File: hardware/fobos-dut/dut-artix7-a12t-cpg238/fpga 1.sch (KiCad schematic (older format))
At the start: 24 parts, among them U1 XC7A12T-CPG238, U9 IS25LP256D-JMLE

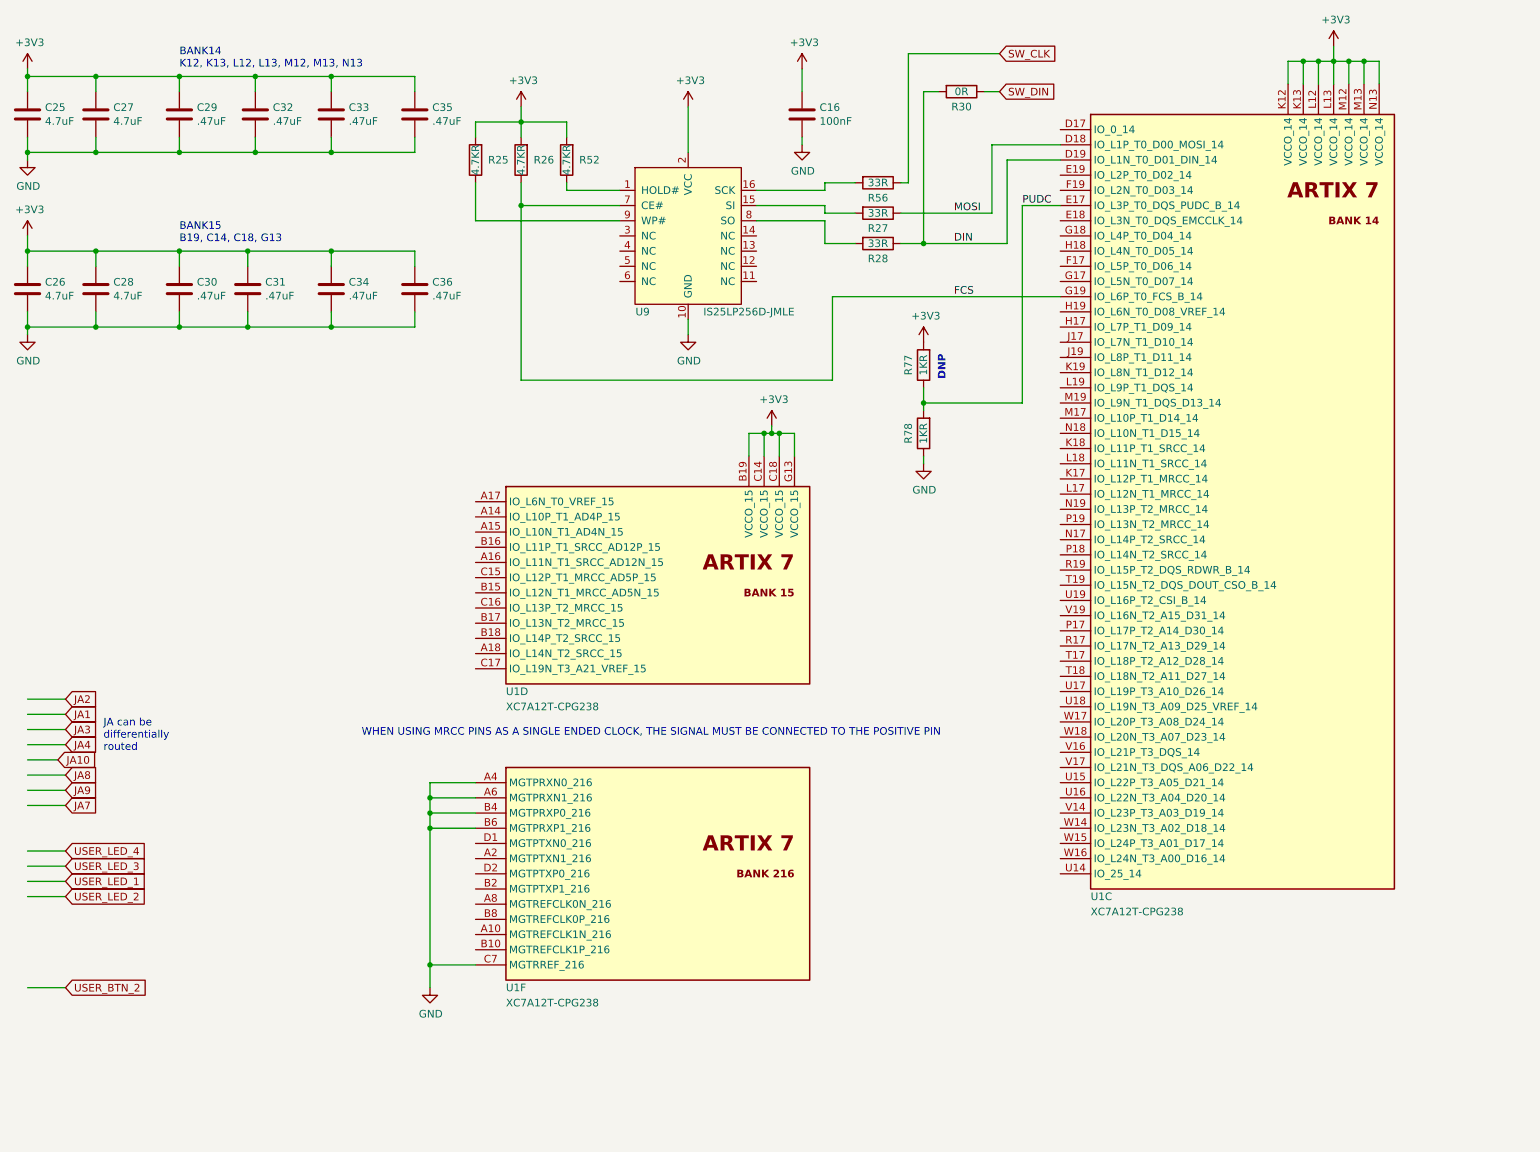
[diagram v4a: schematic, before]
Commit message: Updated escape routing of most pads to take advantage of "pad sacrifices"
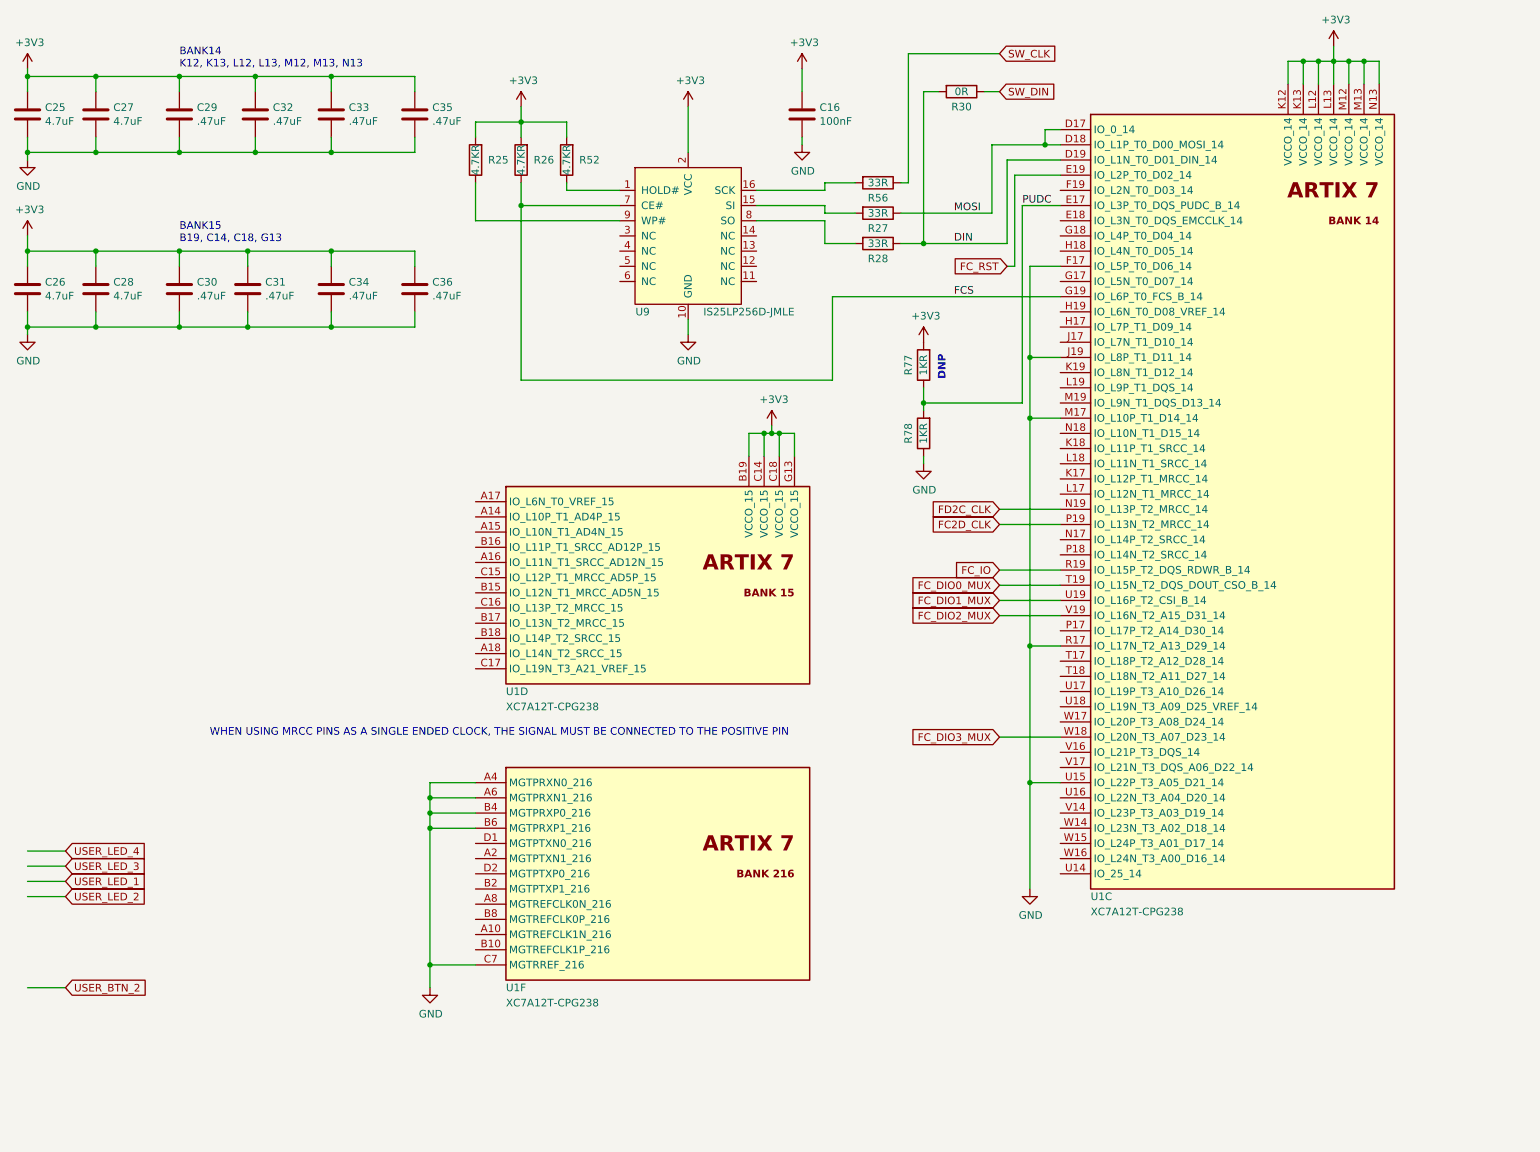
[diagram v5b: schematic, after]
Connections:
- net labels added: FC2D_CLK, FC_DIO0_MUX, FC_DIO1_MUX, FC_DIO2_MUX, FC_DIO3_MUX, FC_IO, FC_RST, FD2C_CLK
- net labels removed: JA1, JA10, JA2, JA3, JA4, JA7, JA8, JA9
- wire segments 142 -> 157
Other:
- note removed: "JA can be \ndifferentially\nrouted"
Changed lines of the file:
@@
 EndData
 $EndBitmap
-Text GLabel 900  5350 2    50   Input ~ 0
-JA1
-Text GLabel 900  5950 2    50   Input ~ 0
-JA7
-Text GLabel 900  5250 2    50   Input ~ 0
-JA2
-Text GLabel 900  5750 2    50   Input ~ 0
-JA8
-Text GLabel 900  5450 2    50   Input ~ 0
-JA3
-Text GLabel 900  5850 2    50   Input ~ 0
-JA9
-Text GLabel 900  5550 2    50   Input ~ 0
-JA4
-Wire Wire Line
-	900  5350 650  5350
-Wire Wire Line
-	650  5950 900  5950
-Wire Wire Line
-	650  5250 900  5250
-Wire Wire Line
-	900  5750 650  5750
-Wire Wire Line
-	900  5450 650  5450
-Wire Wire Line
-	900  5850 650  5850
-Wire Wire Line
-	900  5550 650  5550
-Text Notes 1150 5600 0    50   ~ 0
-JA can be \ndifferentially\nrouted
 $Comp
 L power:GND #PWR0124
@@
 Wire Wire Line
 	5750 1100 5750 1250
-Text GLabel 850  5650 2    50   Input ~ 0
-JA10
-Wire Wire Line
-	850  5650 650  5650
 Text GLabel 900  6250 2    50   Input ~ 0
 USER_LED_4
@@
 	7100 1700 7450 1700
 Wire Wire Line
-	7000 1600 7450 1600
+	7000 1600 7350 1600
 Text Notes 1650 2250 0    50   ~ 0
 BANK15\nB19, C14, C18, G13
@@
 Wire Wire Line
 	3300 7000 3300 7150
-Text Notes 2850 5500 0    50   ~ 0
+Text Notes 1850 5500 0    50   ~ 0
 WHEN USING MRCC PINS AS A SINGLE ENDED CLOCK, THE SIGNAL MUST BE CONNECTED TO THE POSITIVE PIN
 Text Label 6750 2050 0    50   ~ 0
@@
 Text Label 7200 2000 0    50   ~ 0
 PUDC
+Text GLabel 7050 4100 0    50   Input ~ 0
+FC2D_CLK
+Text GLabel 7050 4000 0    50   Input ~ 0
+FD2C_CLK
+Text GLabel 7100 2400 0    50   Input ~ 0
+FC_RST
+Wire Wire Line
+	7100 2400 7150 2400
+Wire Wire Line
+	7150 2400 7150 1800
+Wire Wire Line
+	7150 1800 7450 1800
+Text GLabel 7050 4400 0    50   Input ~ 0
+FC_IO
+Wire Wire Line
+	7050 4400 7450 4400
+Text GLabel 7050 4500 0    50   Input ~ 0
+FC_DIO0_MUX
+Wire Wire Line
+	7050 4500 7450 4500
+Wire Wire Line
+	7050 4000 7450 4000
+Wire Wire Line
+	7050 4100 7450 4100
+Text GLabel 7050 4600 0    50   Input ~ 0
+FC_DIO1_MUX
+Wire Wire Line
+	7450 4600 7050 4600
+Text GLabel 7050 4700 0    50   Input ~ 0
+FC_DIO2_MUX
+Wire Wire Line
+	7450 4700 7050 4700
+Text GLabel 7050 5500 0    50   Input ~ 0
+FC_DIO3_MUX
+Wire Wire Line
+	7450 5500 7050 5500
+$Comp
+L power:GND #PWR?
+U 1 1 61EE39A7
+P 7250 6500
+AR Path="/5F3A1954/61EE39A7" Ref="#PWR?"  Part="1"
+AR Path="/60D2F94F/61EE39A7" Ref="#PWR?"  Part="1"
+AR Path="/5F22D594/61EE39A7" Ref="#PWR0136"  Part="1"
+F 0 "#PWR0136" H 7250 6250 50  0001 C CNN
+F 1 "GND" H 7255 6327 50  0000 C CNN
+F 2 "" H 7250 6500 50  0001 C CNN
+F 3 "" H 7250 6500 50  0001 C CNN
+	1    7250 6500
+	1    0    0    -1
+$EndComp
+Wire Wire Line
+	7450 5800 7250 5800
+Wire Wire Line
+	7250 5800 7250 6500
+Wire Wire Line
+	7450 4900 7250 4900
+Wire Wire Line
+	7250 4900 7250 5800
+Connection ~ 7250 5800
+Wire Wire Line
+	7450 3400 7250 3400
+Wire Wire Line
+	7250 3400 7250 4900
+Connection ~ 7250 4900
+Wire Wire Line
+	7450 3000 7250 3000
+Wire Wire Line
+	7250 3000 7250 3400
+Connection ~ 7250 3400
+Wire Wire Line
+	7450 2400 7250 2400
+Wire Wire Line
+	7250 2400 7250 3000
+Connection ~ 7250 3000
+Wire Wire Line
+	7450 1500 7350 1500
+Wire Wire Line
+	7350 1500 7350 1600
+Connection ~ 7350 1600
+Wire Wire Line
+	7350 1600 7450 1600
 $EndSCHEMATC

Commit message: All signals routed, need to route power
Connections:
- net labels added: FC2D_HS, FD2C_HS, MODE_0, USER_BTN_1
- net labels removed: USER_BTN_2, USER_LED_2, USER_LED_3, USER_LED_4
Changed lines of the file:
@@
 Wire Wire Line
 	5750 1100 5750 1250
-Text GLabel 900  6250 2    50   Input ~ 0
-USER_LED_4
-Wire Wire Line
-	650  6250 900  6250
-Text GLabel 900  6350 2    50   Input ~ 0
-USER_LED_3
-Wire Wire Line
-	650  6350 900  6350
-Text GLabel 900  6550 2    50   Input ~ 0
-USER_LED_2
-Wire Wire Line
-	650  6550 900  6550
-Text GLabel 900  6450 2    50   Input ~ 0
-USER_LED_1
-Wire Wire Line
-	650  6450 900  6450
-Text GLabel 900  7150 2    50   Input ~ 0
-USER_BTN_2
-Wire Wire Line
-	900  7150 650  7150
 $Comp
 L cerg:XC7A12T-CPG238 U1
@@
 Wire Wire Line
 	7350 1600 7450 1600
+Wire Wire Line
+	7450 6100 7050 6100
+Text GLabel 7050 6100 0    50   Input ~ 0
+MODE_0
+Wire Wire Line
+	3350 4150 3600 4150
+Text GLabel 3350 4150 0    50   Input ~ 0
+USER_BTN_1
+Wire Wire Line
+	3600 4050 3350 4050
+Text GLabel 3350 4050 0    50   Input ~ 0
+USER_LED_1
+Text GLabel 7050 5400 0    50   Input ~ 0
+FC2D_HS
+Text GLabel 7050 6300 0    50   Input ~ 0
+FD2C_HS
+Wire Wire Line
+	7050 6300 7450 6300
+Wire Wire Line
+	7050 5400 7450 5400
 $EndSCHEMATC

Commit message: almost last review
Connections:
- net FC2D_CLK: now also U1.N19 (IO_L13P_T2_MRCC_14); no longer U1.P19 (IO_L13N_T2_MRCC_14)
- net FD2C_CLK: now also U1.K17 (IO_L12P_T1_MRCC_14), U1.K18 (IO_L11P_T1_SRCC_14), U1.K19 (IO_L8N_T1_D12_14); no longer U1.N19 (IO_L13P_T2_MRCC_14)
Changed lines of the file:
@@
 Text Label 7200 2000 0    50   ~ 0
 PUDC
-Text GLabel 7050 4100 0    50   Input ~ 0
+Text GLabel 7050 4000 0    50   Input ~ 0
 FC2D_CLK
-Text GLabel 7050 4000 0    50   Input ~ 0
+Text GLabel 7050 3800 0    50   Input ~ 0
 FD2C_CLK
 Text GLabel 7100 2400 0    50   Input ~ 0
@@
 Wire Wire Line
 	7050 4000 7450 4000
-Wire Wire Line
-	7050 4100 7450 4100
 Text GLabel 7050 4600 0    50   Input ~ 0
 FC_DIO1_MUX
@@
 Wire Wire Line
 	7050 5400 7450 5400
+Wire Wire Line
+	7450 3800 7300 3800
+Wire Wire Line
+	7450 3600 7300 3600
+Wire Wire Line
+	7300 3600 7300 3800
+Connection ~ 7300 3800
+Wire Wire Line
+	7300 3800 7050 3800
+Wire Wire Line
+	7450 3100 7300 3100
+Wire Wire Line
+	7300 3100 7300 3600
+Connection ~ 7300 3600
 $EndSCHEMATC
